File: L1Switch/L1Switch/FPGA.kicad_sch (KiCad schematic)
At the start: 9 parts, among them J11 Conn_01x06_Male, U1 XC7A35T-FTG256, X1 LFSPXO076034CUTT

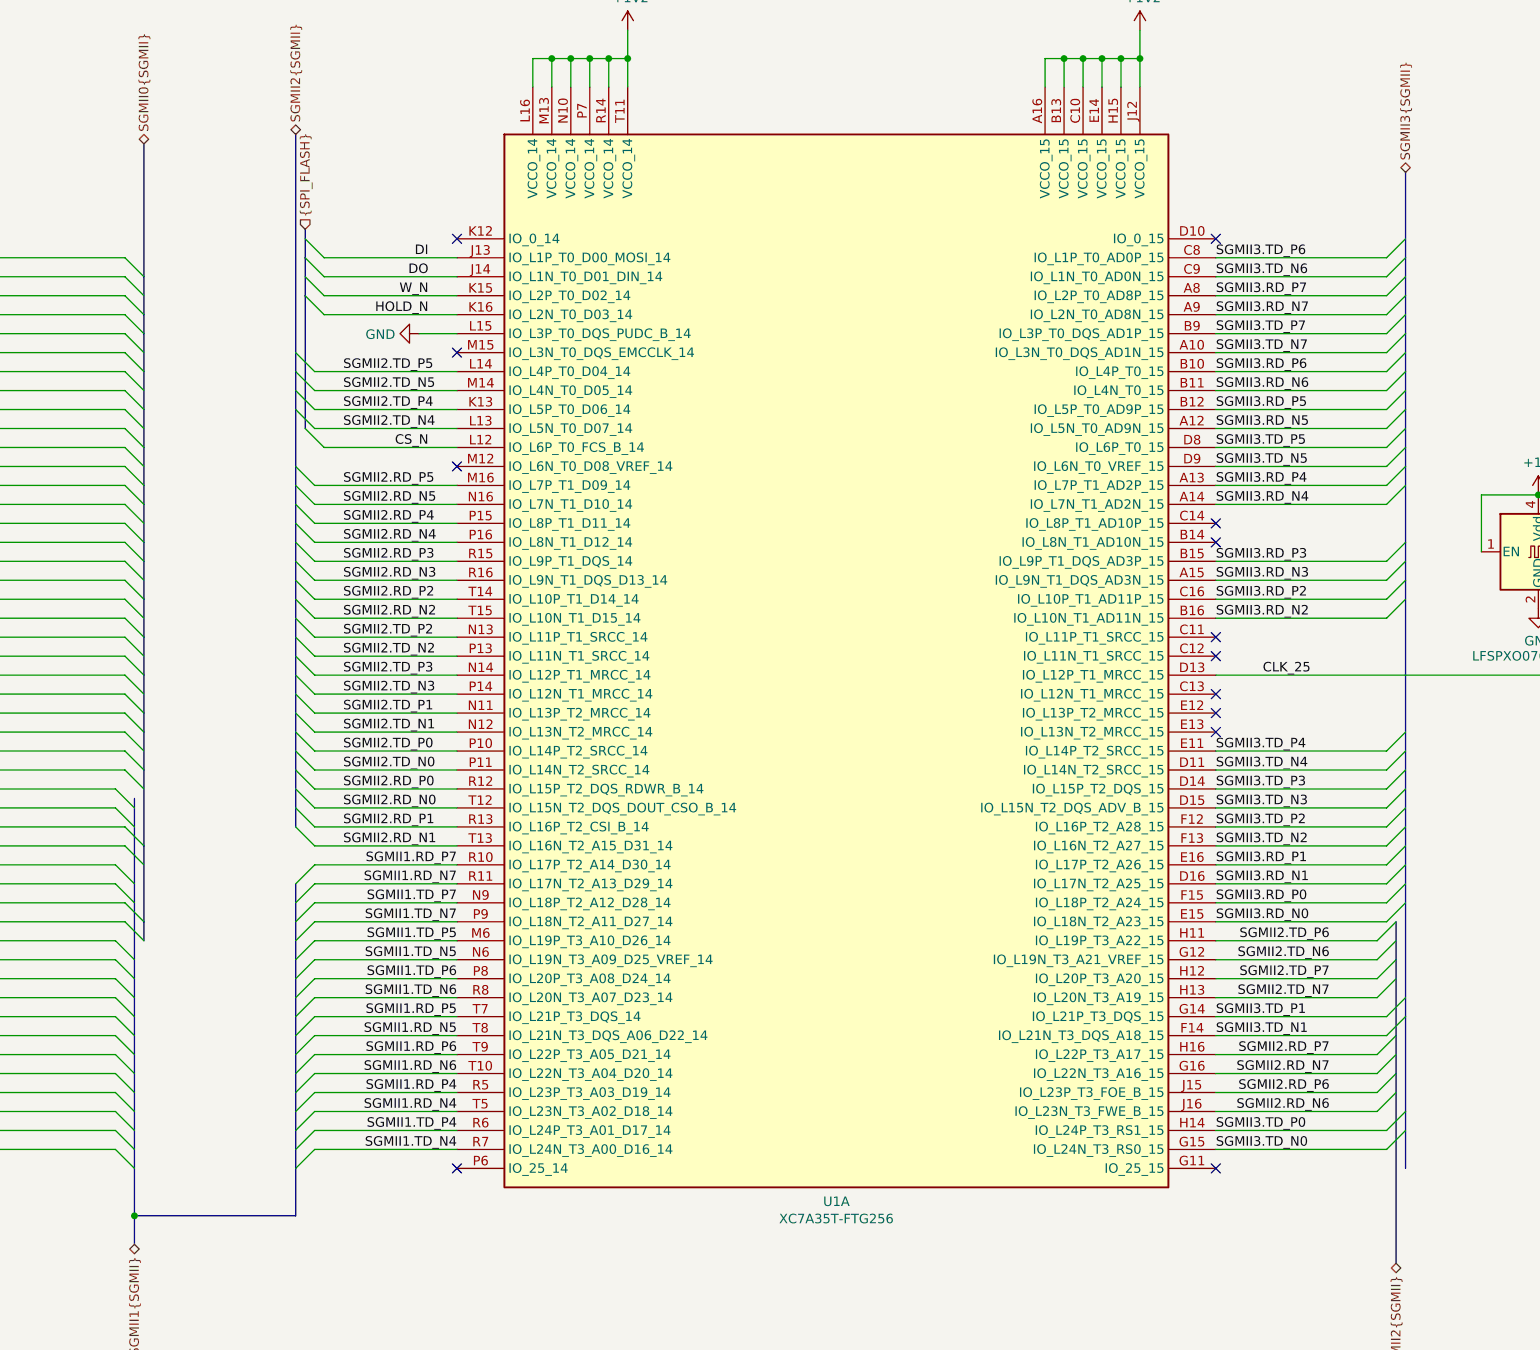
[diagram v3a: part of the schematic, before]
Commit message: Added power-on-reset circuit.
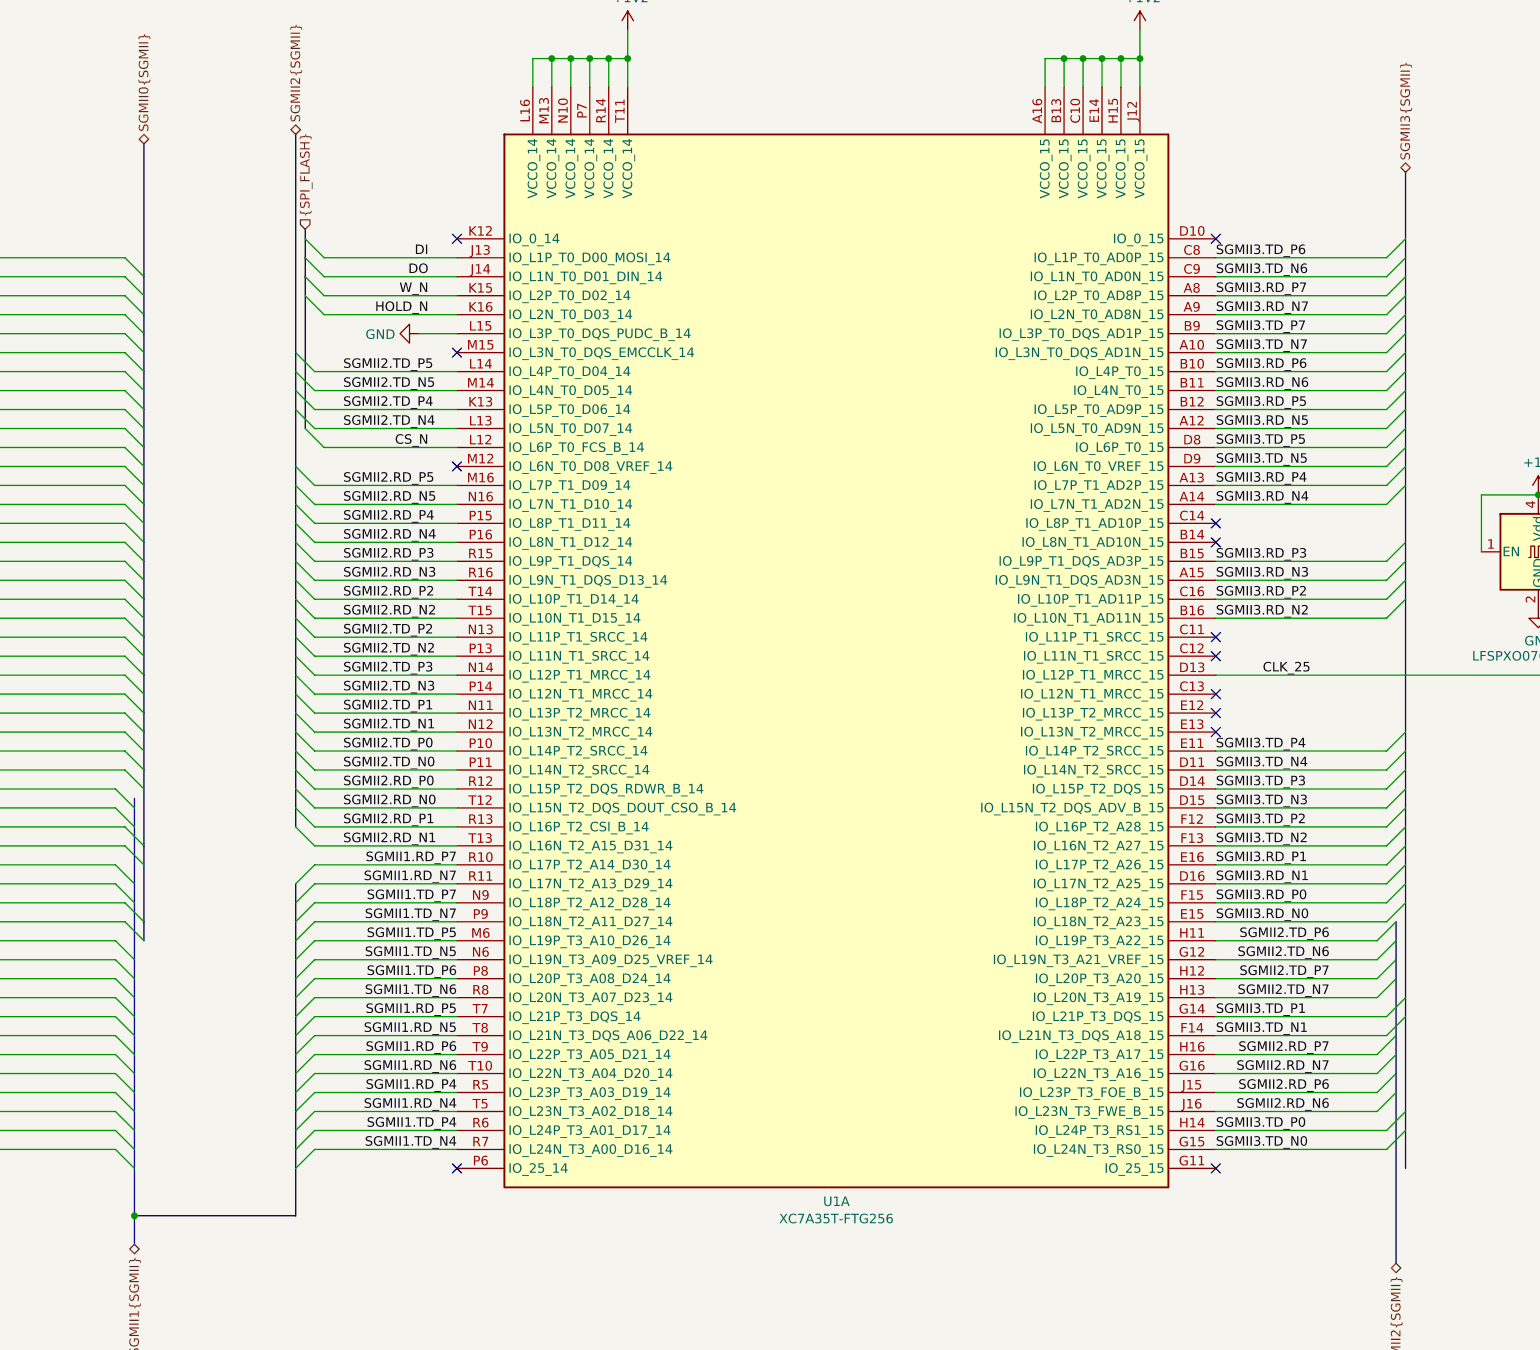
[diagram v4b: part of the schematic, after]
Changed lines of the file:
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@@
   (junction (at 414.02 125.73))
   (junction (at 213.36 198.12))
+  (no_connect (at 358.14 120.65))
   (no_connect (at 358.14 123.19))
-  (no_connect (at 358.14 133.35))
-  (no_connect (at 358.14 120.65))
+  (no_connect (at 46.99 124.46))
+  (no_connect (at 177.8 191.77))
+  (no_connect (at 358.14 107.95))
+  (no_connect (at 256.54 191.77))
+  (no_connect (at 358.14 105.41))
+  (no_connect (at 76.2 115.57))
+  (no_connect (at 358.14 128.27))
+  (no_connect (at 76.2 102.87))
+  (no_connect (at 256.54 97.79))
+  (no_connect (at 76.2 105.41))
+  (no_connect (at 46.99 114.3))
+  (no_connect (at 76.2 107.95))
+  (no_connect (at 177.8 67.31))
+  (no_connect (at 358.14 67.31))
+  (no_connect (at 46.99 116.84))
+  (no_connect (at 358.14 191.77))
   (no_connect (at 358.14 130.81))
-  (no_connect (at 76.2 102.87))
-  (no_connect (at 76.2 115.57))
-  (no_connect (at 358.14 191.77))
-  (no_connect (at 177.8 191.77))
-  (no_connect (at 76.2 107.95))
-  (no_connect (at 358.14 128.27))
-  (no_connect (at 46.99 114.3))
   (no_connect (at 256.54 82.55))
   (no_connect (at 256.54 67.31))
-  (no_connect (at 256.54 191.77))
-  (no_connect (at 256.54 97.79))
-  (no_connect (at 46.99 116.84))
-  (no_connect (at 76.2 105.41))
-  (no_connect (at 358.14 105.41))
-  (no_connect (at 46.99 124.46))
-  (no_connect (at 177.8 67.31))
-  (no_connect (at 358.14 107.95))
-  (no_connect (at 358.14 67.31))
+  (no_connect (at 358.14 133.35))
   (bus_entry (at 210.82 140.97) (size 2.54 2.54))
   (bus_entry (at 210.82 143.51) (size 2.54 2.54))
@@
     (stroke (width 0) (type solid) (color 0 0 0 0))
   )
-  (bus (pts (xy 213.36 146.05) (xy 213.36 156.21))
-    (stroke (width 0) (type solid) (color 0 0 0 0))
-  )
-  (bus (pts (xy 213.36 156.21) (xy 213.36 166.37))
-    (stroke (width 0) (type solid) (color 0 0 0 0))
-  )
-  (bus (pts (xy 213.36 166.37) (xy 213.36 171.45))
-    (stroke (width 0) (type solid) (color 0 0 0 0))
-  )
-  (bus (pts (xy 213.36 171.45) (xy 213.36 176.53))
+  (bus (pts (xy 213.36 146.05) (xy 213.36 153.67))
+    (stroke (width 0) (type solid) (color 0 0 0 0))
+  )
+  (bus (pts (xy 213.36 153.67) (xy 213.36 163.83))
+    (stroke (width 0) (type solid) (color 0 0 0 0))
+  )
+  (bus (pts (xy 213.36 163.83) (xy 213.36 168.91))
+    (stroke (width 0) (type solid) (color 0 0 0 0))
+  )
+  (bus (pts (xy 213.36 168.91) (xy 213.36 173.99))
+    (stroke (width 0) (type solid) (color 0 0 0 0))
+  )
+  (bus (pts (xy 213.36 173.99) (xy 213.36 176.53))
     (stroke (width 0) (type solid) (color 0 0 0 0))
   )
@@
     (stroke (width 0) (type solid) (color 0 0 0 0))
   )
-  (bus (pts (xy 213.36 186.69) (xy 213.36 189.23))
-    (stroke (width 0) (type solid) (color 0 0 0 0))
-  )
-  (bus (pts (xy 213.36 189.23) (xy 213.36 198.12))
+  (bus (pts (xy 213.36 186.69) (xy 213.36 191.77))
+    (stroke (width 0) (type solid) (color 0 0 0 0))
+  )
+  (bus (pts (xy 213.36 191.77) (xy 213.36 198.12))
     (stroke (width 0) (type solid) (color 0 0 0 0))
   )
@@
     (stroke (width 0) (type solid) (color 0 0 0 0))
   )
-  (bus (pts (xy 234.95 53.34) (xy 234.95 85.09))
-    (stroke (width 0) (type solid) (color 0 0 0 0))
-  )
-  (bus (pts (xy 234.95 85.09) (xy 234.95 90.17))
-    (stroke (width 0) (type solid) (color 0 0 0 0))
-  )
-  (bus (pts (xy 234.95 90.17) (xy 234.95 97.79))
+  (bus (pts (xy 234.95 53.34) (xy 234.95 82.55))
+    (stroke (width 0) (type solid) (color 0 0 0 0))
+  )
+  (bus (pts (xy 234.95 82.55) (xy 234.95 87.63))
+    (stroke (width 0) (type solid) (color 0 0 0 0))
+  )
+  (bus (pts (xy 234.95 87.63) (xy 234.95 97.79))
     (stroke (width 0) (type solid) (color 0 0 0 0))
   )
@@
     (stroke (width 0) (type solid) (color 0 0 0 0))
   )
-  (bus (pts (xy 234.95 120.65) (xy 234.95 125.73))
-    (stroke (width 0) (type solid) (color 0 0 0 0))
-  )
-  (bus (pts (xy 234.95 125.73) (xy 234.95 130.81))
-    (stroke (width 0) (type solid) (color 0 0 0 0))
-  )
-  (bus (pts (xy 234.95 130.81) (xy 234.95 133.35))
+  (bus (pts (xy 234.95 120.65) (xy 234.95 123.19))
+    (stroke (width 0) (type solid) (color 0 0 0 0))
+  )
+  (bus (pts (xy 234.95 123.19) (xy 234.95 128.27))
+    (stroke (width 0) (type solid) (color 0 0 0 0))
+  )
+  (bus (pts (xy 234.95 128.27) (xy 234.95 133.35))
     (stroke (width 0) (type solid) (color 0 0 0 0))
   )
@@
     (stroke (width 0) (type solid) (color 0 0 0 0))
   )
-  (bus (pts (xy 234.95 153.67) (xy 234.95 158.75))
-    (stroke (width 0) (type solid) (color 0 0 0 0))
-  )
-  (bus (pts (xy 234.95 158.75) (xy 234.95 163.83))
-    (stroke (width 0) (type solid) (color 0 0 0 0))
-  )
-  (bus (pts (xy 234.95 163.83) (xy 234.95 168.91))
-    (stroke (width 0) (type solid) (color 0 0 0 0))
-  )
-  (bus (pts (xy 234.95 168.91) (xy 234.95 173.99))
+  (bus (pts (xy 234.95 153.67) (xy 234.95 156.21))
+    (stroke (width 0) (type solid) (color 0 0 0 0))
+  )
+  (bus (pts (xy 234.95 156.21) (xy 234.95 161.29))
+    (stroke (width 0) (type solid) (color 0 0 0 0))
+  )
+  (bus (pts (xy 234.95 161.29) (xy 234.95 166.37))
+    (stroke (width 0) (type solid) (color 0 0 0 0))
+  )
+  (bus (pts (xy 234.95 166.37) (xy 234.95 171.45))
+    (stroke (width 0) (type solid) (color 0 0 0 0))
+  )
+  (bus (pts (xy 234.95 171.45) (xy 234.95 173.99))
     (stroke (width 0) (type solid) (color 0 0 0 0))
   )
@@
     (stroke (width 0) (type solid) (color 0 0 0 0))
   )
-  (bus (pts (xy 234.95 179.07) (xy 234.95 181.61))
-    (stroke (width 0) (type solid) (color 0 0 0 0))
-  )
-  (bus (pts (xy 234.95 181.61) (xy 234.95 186.69))
-    (stroke (width 0) (type solid) (color 0 0 0 0))
-  )
-  (bus (pts (xy 234.95 186.69) (xy 234.95 191.77))
-    (stroke (width 0) (type solid) (color 0 0 0 0))
-  )
-  (bus (pts (xy 234.95 191.77) (xy 234.95 198.12))
+  (bus (pts (xy 234.95 179.07) (xy 234.95 184.15))
+    (stroke (width 0) (type solid) (color 0 0 0 0))
+  )
+  (bus (pts (xy 234.95 184.15) (xy 234.95 189.23))
+    (stroke (width 0) (type solid) (color 0 0 0 0))
+  )
+  (bus (pts (xy 234.95 189.23) (xy 234.95 198.12))
     (stroke (width 0) (type solid) (color 0 0 0 0))
   )
@@
     (stroke (width 0) (type solid) (color 0 0 0 0))
   )
-  (bus (pts (xy 236.22 69.85) (xy 236.22 74.93))
-    (stroke (width 0) (type solid) (color 0 0 0 0))
-  )
-  (bus (pts (xy 236.22 74.93) (xy 236.22 92.71))
+  (bus (pts (xy 236.22 69.85) (xy 236.22 72.39))
+    (stroke (width 0) (type solid) (color 0 0 0 0))
+  )
+  (bus (pts (xy 236.22 72.39) (xy 236.22 92.71))
     (stroke (width 0) (type solid) (color 0 0 0 0))
   )
@@
     (stroke (width 0) (type solid) (color 0 0 0 0))
   )
-  (bus (pts (xy 383.54 95.25) (xy 383.54 97.79))
-    (stroke (width 0) (type solid) (color 0 0 0 0))
-  )
-  (bus (pts (xy 383.54 97.79) (xy 383.54 107.95))
-    (stroke (width 0) (type solid) (color 0 0 0 0))
-  )
-  (bus (pts (xy 383.54 107.95) (xy 383.54 113.03))
-    (stroke (width 0) (type solid) (color 0 0 0 0))
-  )
-  (bus (pts (xy 383.54 113.03) (xy 383.54 133.35))
-    (stroke (width 0) (type solid) (color 0 0 0 0))
-  )
-  (bus (pts (xy 383.54 133.35) (xy 383.54 138.43))
+  (bus (pts (xy 383.54 95.25) (xy 383.54 100.33))
+    (stroke (width 0) (type solid) (color 0 0 0 0))
+  )
+  (bus (pts (xy 383.54 100.33) (xy 383.54 110.49))
+    (stroke (width 0) (type solid) (color 0 0 0 0))
+  )
+  (bus (pts (xy 383.54 110.49) (xy 383.54 115.57))
+    (stroke (width 0) (type solid) (color 0 0 0 0))
+  )
+  (bus (pts (xy 383.54 115.57) (xy 383.54 135.89))
+    (stroke (width 0) (type solid) (color 0 0 0 0))
+  )
+  (bus (pts (xy 383.54 135.89) (xy 383.54 138.43))
     (stroke (width 0) (type solid) (color 0 0 0 0))
   )
@@
     (stroke (width 0) (type solid) (color 0 0 0 0))
   )
-  (bus (pts (xy 383.54 148.59) (xy 383.54 151.13))
-    (stroke (width 0) (type solid) (color 0 0 0 0))
-  )
-  (bus (pts (xy 383.54 151.13) (xy 383.54 156.21))
-    (stroke (width 0) (type solid) (color 0 0 0 0))
-  )
-  (bus (pts (xy 383.54 156.21) (xy 383.54 171.45))
-    (stroke (width 0) (type solid) (color 0 0 0 0))
-  )
-  (bus (pts (xy 383.54 171.45) (xy 383.54 184.15))
-    (stroke (width 0) (type solid) (color 0 0 0 0))
-  )
+  (bus (pts (xy 383.54 148.59) (xy 383.54 153.67))
+    (stroke (width 0) (type solid) (color 0 0 0 0))
+  )
+  (bus (pts (xy 383.54 153.67) (xy 383.54 168.91))
+    (stroke (width 0) (type solid) (color 0 0 0 0))
+  )
+  (bus (pts (xy 383.54 168.91) (xy 383.54 184.15))
+    (stroke (width 0) (type solid) (color 0 0 0 0))
+  )
